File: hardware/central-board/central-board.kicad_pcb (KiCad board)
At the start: 2 copper layers, 267.6 x 146.6 mm, 64 parts, among them J1 MTJ-88ARX1-FSM-LG, J10 Conn_01x02, J11 Conn_01x02, J12 IO I2C Bus, J2 1729128, J3 1729128, J4 RPi_GPIO, J5 PEC11R, J7 GPIO Bus, J8 Conn_01x02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

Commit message: updates to primary
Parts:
- moved J7 91.2 mm to (124.3, 20.2)
- moved J5 90.6 mm to (144.2, 21.5)
- moved L1 69.0 mm to (141.3, 70.4), turned to 0 degrees
- moved R5 67.2 mm to (145.8, 64.0), turned to 180 degrees
- moved U5 66.0 mm to (146.2, 47.6)
- moved Q3 65.5 mm to (134.2, 79.9), turned to -90 degrees
- moved R6 65.2 mm to (144.3, 63.5), turned to 90 degrees
- moved C10 62.0 mm to (146.3, 57.1), turned to 90 degrees
- moved J12 61.4 mm to (123.0, 49.7), turned to 180 degrees
- moved C13 61.1 mm to (130.8, 63.9), turned to 0 degrees
- moved Q2 60.6 mm to (137.8, 79.9), turned to -90 degrees
- moved D2 59.7 mm to (131.0, 68.2), turned to 90 degrees
- moved U6 59.4 mm to (141.0, 61.1), turned to 90 degrees
- moved C9 59.1 mm to (137.4, 64.4), turned to 180 degrees
- moved L2 56.4 mm to (124.4, 58.0), turned to 180 degrees
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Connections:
- J4 pad 36: VBUS_EN -> unconnected-(J4-BCM16-Pad36)
- U4 pad 5: VBUS_EN -> unconnected-(U4-ENA-Pad5)
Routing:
- net +12V: track 23.3 -> 95.9 mm, vias 1 -> 6
- net +5V: track 0.00 -> 64.4 mm, vias 0 -> 2
- net +24V: track 12.4 -> 55.6 mm, vias 0 -> 10
- net Net-(Q3-G): track 0.00 -> 19.0 mm, vias 0 -> 2
- net Net-(Q5-G): track 0.00 -> 15.3 mm, vias 0 -> 2
- net Net-(Q2-G): track 0.00 -> 14.7 mm, vias 0 -> 2
- net SDA: track 0.00 -> 12.6 mm
- net SCL: track 0.00 -> 12.6 mm
- net Net-(Q6-G): track 0.00 -> 12.3 mm, vias 0 -> 2
- net Net-(Q1-G): track 0.00 -> 10.5 mm, vias 0 -> 2
- net Net-(Q4-G): track 0.00 -> 7.80 mm, vias 0 -> 2
- net Net-(J1-Pad6): track 0.00 -> 6.89 mm, vias 0 -> 1
- net Net-(J8-Pin_2): track 0.00 -> 3.00 mm
- net Net-(J11-Pin_2): track 0.00 -> 3.00 mm
- net Net-(J10-Pin_2): track 0.00 -> 3.00 mm
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- added copper zone on B.Cu, net +12V
- added copper zone on B.Cu, net +24V
- added copper zone on F.Cu, net -LED
- added copper zone on B.Cu, net GND

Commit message: more updates
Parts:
- removed J9: IO Power Bus, Connector_PinHeader_2.54mm:PinHeader_2x05_P2.54mm_Vertical
- added J6: IO Power Bus, Connector_PinHeader_2.54mm:PinHeader_2x03_P2.54mm_Vertical, F.Cu at (136.7, 48.7)
- J7: footprint Connector_PinHeader_2.54mm:PinHeader_2x03_P2.54mm_Vertical -> Connector_PinHeader_2.54mm:PinHeader_1x06_P2.54mm_Vertical
- moved C6 98.3 mm to (129.0, 49.8), turned to 180 degrees
- moved C5 93.9 mm to (128.9, 44.0), turned to 180 degrees
- moved C4 65.3 mm to (163.7, 64.5), turned to 180 degrees
- moved C3 61.9 mm to (163.7, 65.9), turned to 180 degrees
- moved C2 55.8 mm to (178.8, 53.5), turned to -90 degrees
- moved C1 47.0 mm to (177.6, 53.5), turned to -90 degrees
- moved J7 41.3 mm to (159.0, 42.6), turned to 90 degrees
- moved U5 17.7 mm to (128.5, 47.1), turned to -90 degrees
- moved R15 13.6 mm to (186.9, 77.2)
- moved R13 11.1 mm to (191.3, 74.2)
- moved U2 4.13 mm to (167.6, 54.1)
- moved U3 4.13 mm to (175.7, 67.1)
- moved R1 2.28 mm to (166.8, 69.5)
- moved U1 1.84 mm to (162.4, 69.4)
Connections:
- J4 pad 11: GPIO17 -> EN_S3
- J4 pad 12: GPIO18 -> RJ45_SNS
- J4 pad 13: EN_S2 -> unconnected-(J4-BCM27-Pad13)
- J4 pad 15: EN_S3 -> unconnected-(J4-BCM22-Pad15)
- J4 pad 16: DIO1 -> unconnected-(J4-BCM23-Pad16)
- J4 pad 18: BUSY -> unconnected-(J4-BCM24-Pad18)
- J4 pad 22: EN_S1 -> unconnected-(J4-BCM25-Pad22)
- J4 pad 29: LED_GRN -> GPIO21
- J4 pad 31: LED_YLW -> GPIO20
- J4 pad 33: RJ45_SNS -> GPIO18
- J4 pad 36: unconnected-(J4-BCM16-Pad36) -> GPIO17
- J4 pad 38: GPIO20 -> BUSY
- J4 pad 40: GPIO21 -> DIO1
- J4 pad 7: unconnected-(J4-BCM4_GPCLK0-Pad7) -> EN_S2
- J4 pad 8: unconnected-(J4-BCM14_TXD-Pad8)_1 -> EN_S1
- J7 pad 1: GPIO26 -> GPIO21
- J7 pad 2: GPIO17 -> GPIO20
- J7 pad 5: GPIO20 -> GPIO17
- J7 pad 6: GPIO21 -> GPIO26
- U4 pad 10: GND -> (no net)
- U4 pad 11: GND -> (no net)
- U4 pad 12: GND -> (no net)
- U4 pad 13: GND -> (no net)
- U4 pad 14: GND -> (no net)
- U4 pad 15: GND -> (no net)
- U4 pad 16: GND -> (no net)
- U4 pad 17: GND -> (no net)
- U6 pad 10: GND -> (no net)
- U6 pad 11: GND -> (no net)
- U6 pad 12: GND -> (no net)
- U6 pad 13: GND -> (no net)
- U6 pad 14: GND -> (no net)
- U6 pad 15: GND -> (no net)
- U6 pad 16: GND -> (no net)
- U6 pad 17: GND -> (no net)
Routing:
- net +3V3: track 0.00 -> 73.0 mm, vias 0 -> 15
- net EN_S1: track 0.00 -> 65.7 mm
- net EN_S2: track 0.00 -> 62.2 mm
- net RS_RX: track 0.00 -> 50.7 mm, vias 0 -> 2
- net EN_S3: track 0.00 -> 46.8 mm
- net GND: track 32.2 -> 62.1 mm, vias 13 -> 85
- net RJ45_SNS: track 0.00 -> 24.4 mm, vias 0 -> 1
- net +5V: track 64.4 -> 83.4 mm, vias 2 -> 13
- net MOSI: track 0.00 -> 18.0 mm
- net LED_GRN: track 0.00 -> 17.4 mm
- net SCK: track 0.00 -> 17.4 mm, vias 0 -> 1
- net DIO1: track 0.00 -> 15.5 mm
- net RS_A: track 0.00 -> 14.9 mm, vias 0 -> 1
- net MISO: track 0.00 -> 14.6 mm
- net BUSY: track 0.00 -> 14.5 mm
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- added copper zone on B.Cu, net +3V3
- added copper zone on F.Cu, net +3V3
- added copper zone on B.Cu, net +5V

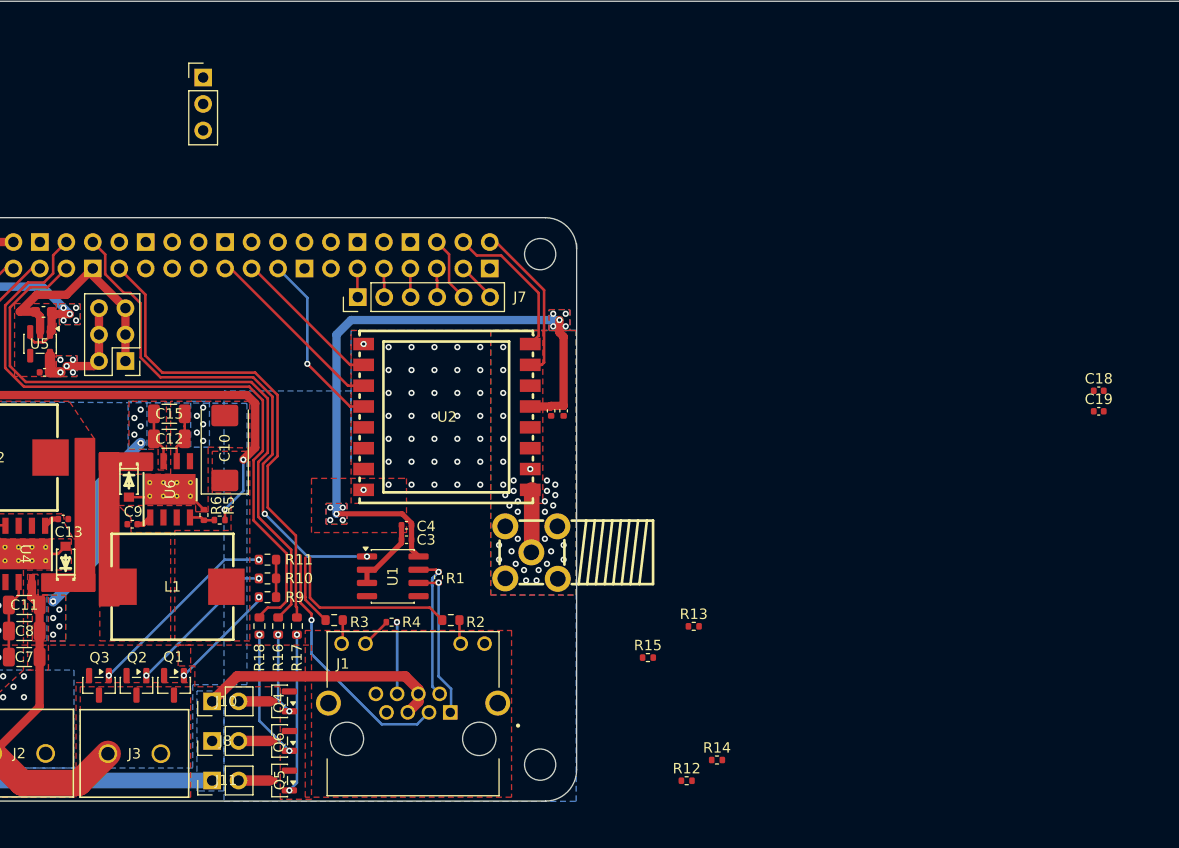
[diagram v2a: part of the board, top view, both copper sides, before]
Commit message: All primary components mounted
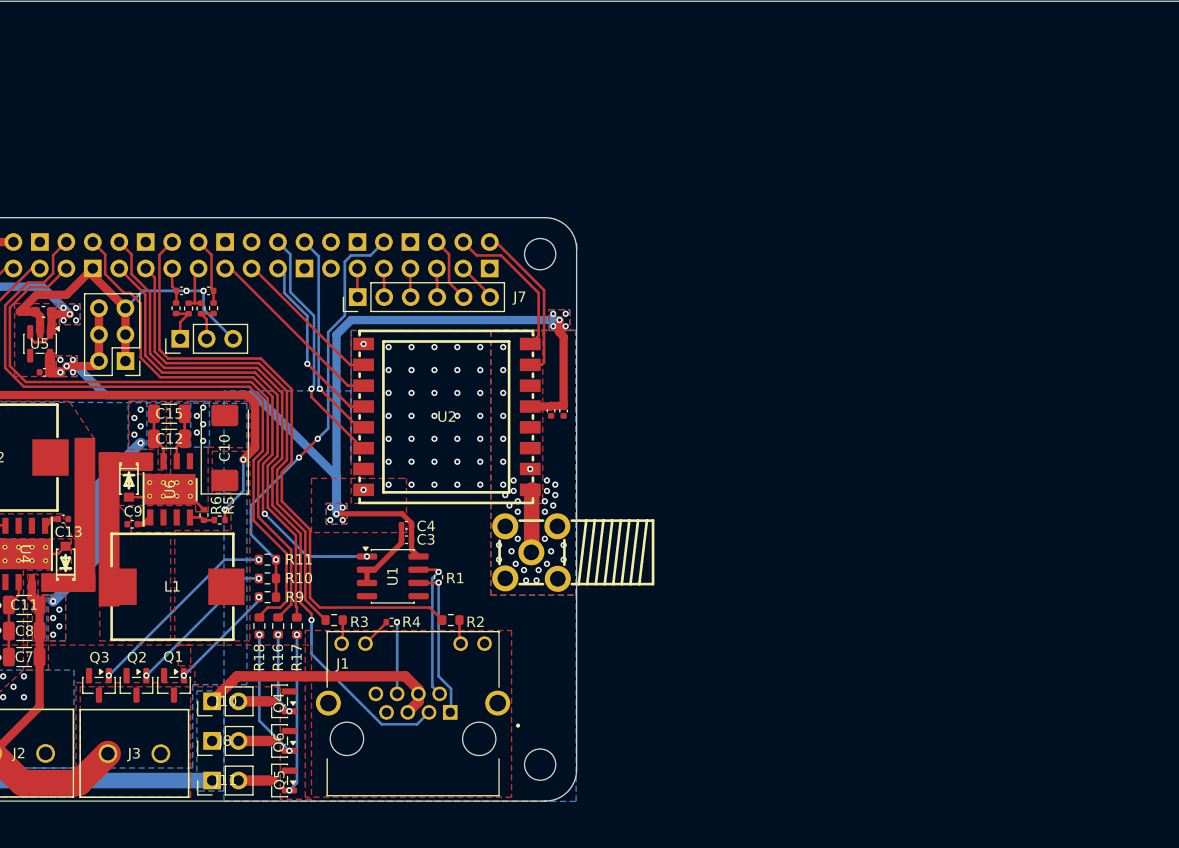
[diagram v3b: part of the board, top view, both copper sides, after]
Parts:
- moved C19 88.8 mm to (142.1, 42.0)
- moved C18 86.0 mm to (144.7, 42.0), turned to 180 degrees
- moved R14 67.6 mm to (141.6, 43.7), turned to -90 degrees
- moved R12 65.9 mm to (142.8, 43.7), turned to -90 degrees
- moved R13 56.3 mm to (144.0, 43.7), turned to -90 degrees
- moved R15 53.5 mm to (145.2, 43.7), turned to -90 degrees
- moved J5 25.2 mm to (142.0, 46.6), turned to 90 degrees
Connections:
- J4 pad 13: unconnected-(J4-BCM27-Pad13) -> LED_YLW
- J4 pad 15: unconnected-(J4-BCM22-Pad15) -> KNOB_A
- J4 pad 16: unconnected-(J4-BCM23-Pad16) -> LED_GRN
- J4 pad 17: unconnected-(J4-3.3V-Pad17)_1 -> ROT_PWR
- J4 pad 18: unconnected-(J4-BCM24-Pad18) -> KNOB_B
- J4 pad 24: CS_1 -> NRESET
- J4 pad 26: NRESET -> CS_1
- R12 pad 1: +3V3 -> ROT_PWR
- R13 pad 1: +3V3 -> ROT_PWR
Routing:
- net RJ45_SNS: track 24.4 -> 67.7 mm
- net LED_GRN: track 17.4 -> 60.2 mm
- net LED_YLW: track 6.81 -> 46.9 mm
- net PWM: track 3.60 -> 41.5 mm, vias 0 -> 3
- net +3V3: track 73.0 -> 106.9 mm
- net NRESET: track 0.00 -> 23.4 mm, vias 0 -> 1
- net CS_1: track 0.00 -> 20.4 mm, vias 0 -> 1
- net GND: track 62.1 -> 76.1 mm, vias 85 -> 87
- net KNOB_B: track 0.00 -> 6.44 mm
- net ROT_PWR: track 0.00 -> 4.68 mm
- net Net-(J5-Pin_1): track 0.00 -> 3.94 mm
- net Net-(J5-Pin_2): track 0.00 -> 3.83 mm
- net KNOB_A: track 0.00 -> 3.49 mm

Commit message: Updates to Fill
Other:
- board size 267.6 x 146.6 mm -> 65 x 56 mm
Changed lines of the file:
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@@
 		(net 6)
 	)
-	(gr_rect
-		(start 14.6 14.2)
-		(end 282.2 160.8)
-		(stroke
-			(width 0.05)
-			(type default)
-		)
-		(fill no)
-		(layer "Edge.Cuts")
-	)
 	(segment
 		(start 134.2 46.2)
@@
 			)
 		)
+	)
+	(zone
+		(net 2)
+		(net_name "GND")
+		(layers "F.Cu" "B.Cu")
+		(hatch edge 0.5)
+		(connect_pads yes
+			(clearance 0.4)
+		)
+		(min_thickness 0.25)
+		(filled_areas_thickness no)
+		(fill yes
+			(thermal_gap 0.5)
+			(thermal_bridge_width 0.5)
+			(smoothing fillet)
+		)
+		(polygon
+			(pts
+				(xy 115 35) (xy 180.2 35) (xy 180 91) (xy 115 91)
+			)
+		)

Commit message: No more errors!
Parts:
- moved R4 1.28 mm to (161.0, 73.8)
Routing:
- net Net-(Q3-G): track 19.0 -> 23.7 mm
- net Net-(Q2-G): track 14.7 -> 18.5 mm
- net GND: track 76.1 -> 78.9 mm, vias 87 -> 94
- net Net-(Q1-G): track 10.5 -> 12.8 mm
- net RS_A: track 14.9 -> 16.6 mm
- net RS_B: track 14.3 -> 15.9 mm
- net Net-(J1-Pad6): track 6.89 -> 8.17 mm
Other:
- outline, holes or cut-outs redrawn

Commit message: Primary prepared for order
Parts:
- C14, C16, C17: footprint Capacitor_Tantalum_SMD:CP_EIA-7343-15_Kemet-W -> Library2:CAP-SMD_L3.5-W2.8-R-RD
- moved C14 45.3 mm to (76.8, 65.6), turned to 180 degrees
- moved C16 43.6 mm to (76.8, 75.6), turned to 180 degrees
- moved C17 43.3 mm to (76.8, 70.6), turned to 180 degrees
- moved C2 43.2 mm to (135.7, 50.3)
- moved C10 43.2 mm to (103.1, 53.9)
- moved C11 43.2 mm to (83.9, 69.0)
- moved C13 43.2 mm to (87.6, 60.7)
- moved C19 43.2 mm to (99.0, 38.8)
- moved C6 43.2 mm to (85.8, 46.6)
- moved C7 43.2 mm to (83.9, 74.0)
- moved C8 43.2 mm to (83.9, 71.5)
- moved J4 43.2 mm to (104.4, 35.3)
- moved J6 43.2 mm to (93.6, 45.5)
- moved L2 43.2 mm to (81.2, 54.8)
- moved Q1 43.2 mm to (98.3, 76.7)
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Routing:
- net Net-(Q3-G): track 23.7 -> 22.8 mm
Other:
- board text added: "Designed by Michael Danley"
- board text added: "ORCA SATELLITE ONLY VIA RJ45!"
- board text added: "Pi 3B Controller IO Hat"
- board text added: "Project ORCA - CENTRAL"

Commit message: Prepared for production
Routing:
- net GND: track 78.9 -> 155.5 mm
